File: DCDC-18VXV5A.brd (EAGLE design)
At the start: 40 x 24 mm, 36 parts, among them Q10 NMOSFET, Q9 NMOSFET, U1 LM3150MHX/NOPB

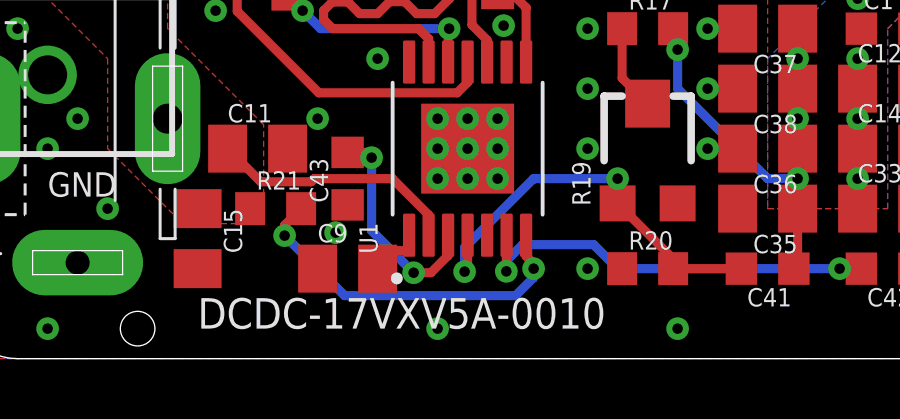
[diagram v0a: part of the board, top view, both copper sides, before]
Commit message: Changed texts on 18V-12V boards. Generated CAM files. Generated PNG preview. Generated PDF schematics.
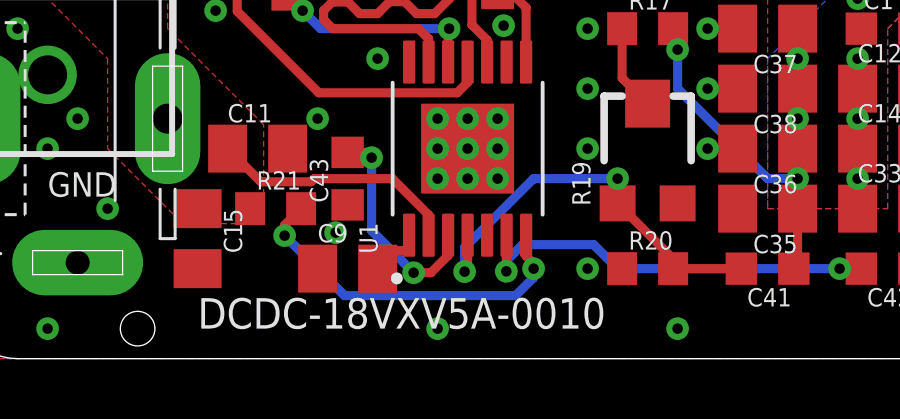
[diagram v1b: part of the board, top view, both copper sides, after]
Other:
- board text added: "DCDC-18VXV5A-0010"
- board text removed: "DCDC-17VXV5A-0010"
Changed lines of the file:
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@@
 <drawing>
 <settings>
-<setting alwaysvectorfont="yes"/>
+<setting alwaysvectorfont="no"/>
 <setting verticaltext="up"/>
 </settings>
@@
 <hole x="37" y="21" drill="3.1"/>
 <hole x="37" y="3" drill="3.1"/>
-<text x="33" y="20" size="1.6764" layer="22" font="vector" ratio="20" rot="MR0">DCDC-17VXV5A-0010</text>
+<text x="33" y="20" size="1.6764" layer="22" font="vector" ratio="20" rot="MR0">DCDC-18VXV5A-0010</text>
 <text x="0.8" y="17.8" size="0.8128" layer="21" font="vector">VIN</text>
 <text x="3" y="5.4" size="0.8128" layer="21" font="vector">GND</text>
@@
 <text x="23" y="17" size="0.8128" layer="21" font="vector" ratio="20">(c) 2021
 Andriy Golovnya</text>
-<text x="8" y="1" size="1.016" layer="21" font="vector">DCDC-17VXV5A-0010</text>
+<text x="8" y="1" size="1.016" layer="21" font="vector">DCDC-18VXV5A-0010</text>
 </plain>
 <attributes>

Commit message: Renamed VOUT line. Generated CAM files. Generated PNG preview. Generated PDF schematics.
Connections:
- net 5V renamed VOUT
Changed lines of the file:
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@@
 <drawing>
 <settings>
-<setting alwaysvectorfont="no"/>
+<setting alwaysvectorfont="yes"/>
 <setting verticaltext="up"/>
 </settings>
@@
 <via x="29" y="18" extent="1-16" drill="0.35"/>
 </signal>
-<signal name="5V" airwireshidden="yes">
+<signal name="VOUT" airwireshidden="yes">
 <contactref element="C36" pad="1"/>
 <contactref element="C38" pad="1"/>
